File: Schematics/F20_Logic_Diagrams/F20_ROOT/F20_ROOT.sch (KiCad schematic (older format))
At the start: 0 parts

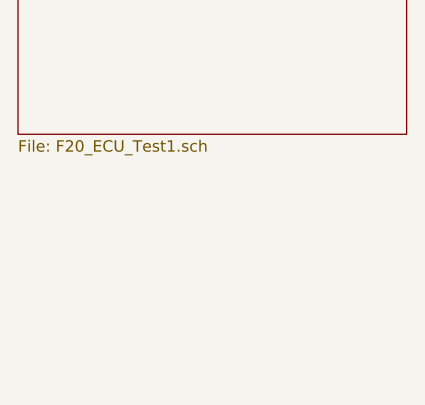
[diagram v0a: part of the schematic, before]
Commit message: Added Driver Display schematic. Added relevant symbols.
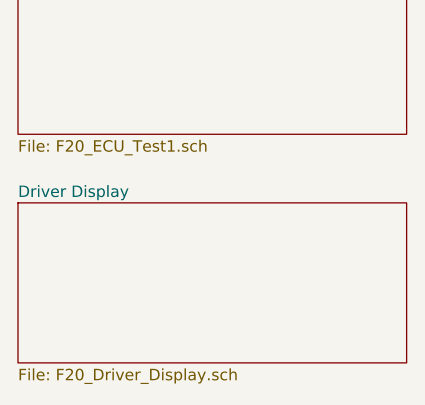
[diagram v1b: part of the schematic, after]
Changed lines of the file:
@@
 EESchema Schematic File Version 4
-LIBS:F20_ROOT-cache
 EELAYER 30 0
 EELAYER END
 $Descr A4 11693 8268
 encoding utf-8
-Sheet 1 4
+Sheet 1 5
 Title "Root Index"
 Date ""
@@
 F1 "F20_ECU_Test1.sch" 50
 $EndSheet
+$Sheet
+S 1000 4000 1700 700
+U 5E28FC41
+F0 "Driver Display" 50
+F1 "F20_Driver_Display.sch" 50
+$EndSheet
 $EndSCHEMATC

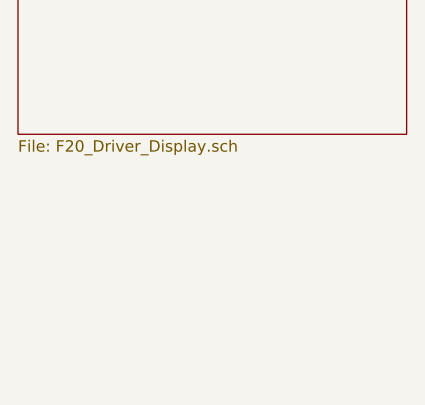
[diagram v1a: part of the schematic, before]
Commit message: Added Brakes logic diagram draft, finished charging/starting schematic portion, added relevant library parts, updated README.
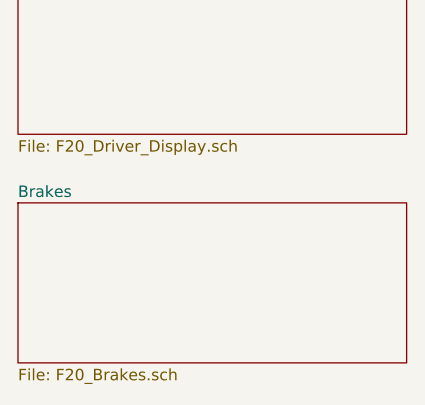
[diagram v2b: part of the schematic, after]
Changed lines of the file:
@@
 EESchema Schematic File Version 4
+LIBS:F20_ROOT-cache
 EELAYER 30 0
 EELAYER END
 $Descr A4 11693 8268
 encoding utf-8
-Sheet 1 5
+Sheet 1 6
 Title "Root Index"
 Date ""
@@
 F1 "F20_Driver_Display.sch" 50
 $EndSheet
+$Sheet
+S 1000 5000 1700 700
+U 5E30D161
+F0 "Brakes" 50
+F1 "F20_Brakes.sch" 50
+$EndSheet
 $EndSCHEMATC

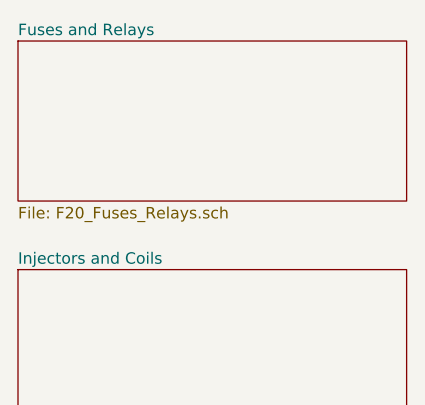
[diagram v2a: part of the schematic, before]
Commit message: Updated Brakes diagram. Updated power management diagram. Updated relevant library symbols. Updated README.
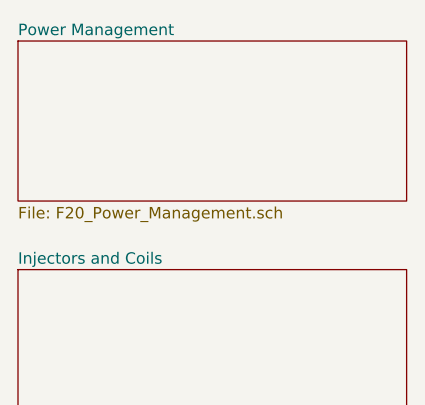
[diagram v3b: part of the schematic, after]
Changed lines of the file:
@@
 $Descr A4 11693 8268
 encoding utf-8
-Sheet 1 6
+Sheet 1 7
 Title "Root Index"
 Date ""
@@
 Comment4 ""
 $EndDescr
-$Sheet
-S 1000 1000 1700 700
-U 5E1D1A8A
-F0 "Fuses and Relays" 50
-F1 "F20_Fuses_Relays.sch" 50
-$EndSheet
 $Sheet
 S 1000 2000 1700 700
@@
 F1 "F20_Brakes.sch" 50
 $EndSheet
+$Sheet
+S 1000 1000 1700 700
+U 5E1D1A8A
+F0 "Power Management" 50
+F1 "F20_Power_Management.sch" 50
+$EndSheet
 $EndSCHEMATC

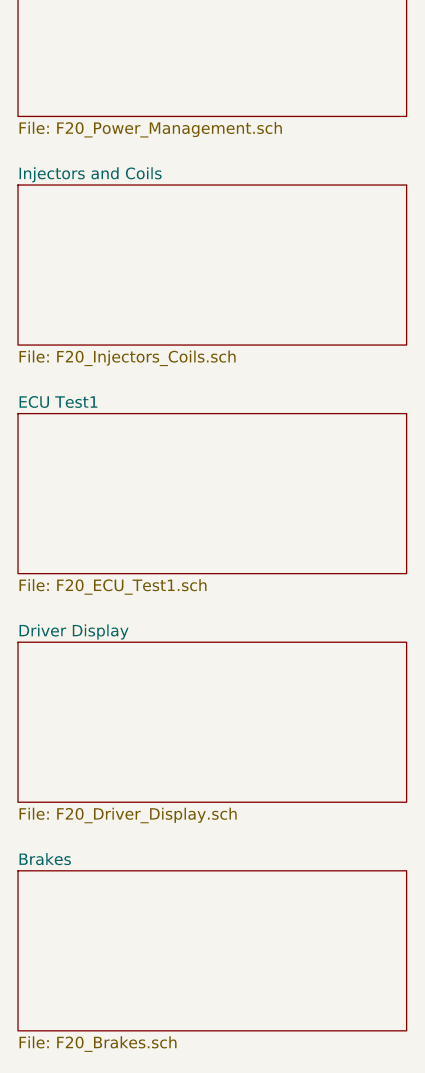
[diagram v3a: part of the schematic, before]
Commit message: Added GND and GND_CHASSIS symbols, updated relevant schematics. Restructured Powertrain hierarchy. Created ECU Connector symbols.
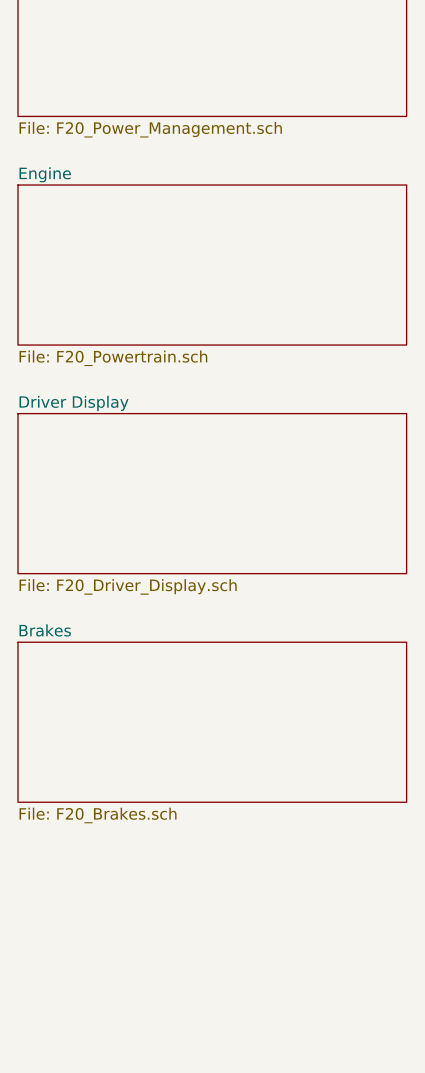
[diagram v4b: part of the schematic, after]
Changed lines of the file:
@@
 S 1000 2000 1700 700
 U 5E1D1B45
-F0 "Injectors and Coils" 50
-F1 "F20_Injectors_Coils.sch" 50
+F0 "Engine" 50
+F1 "F20_Powertrain.sch" 50
 $EndSheet
 $Sheet
 S 1000 3000 1700 700
-U 5E1D1BB2
-F0 "ECU Test1" 50
-F1 "F20_ECU_Test1.sch" 50
-$EndSheet
-$Sheet
-S 1000 4000 1700 700
 U 5E28FC41
 F0 "Driver Display" 50
@@
 $EndSheet
 $Sheet
-S 1000 5000 1700 700
+S 1000 4000 1700 700
 U 5E30D161
 F0 "Brakes" 50

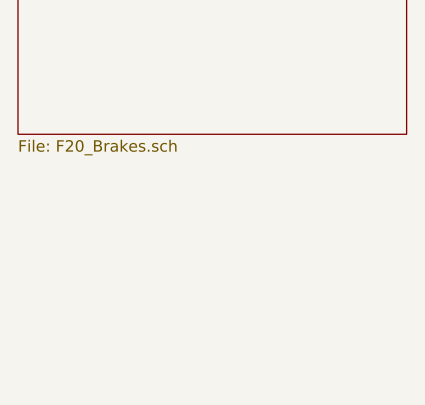
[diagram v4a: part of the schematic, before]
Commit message: Updated per AD commit. O2 sensor schematic, transponder schematic.
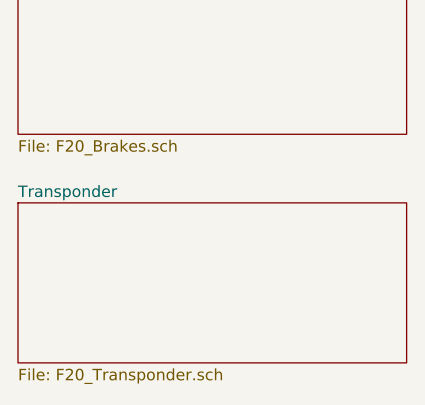
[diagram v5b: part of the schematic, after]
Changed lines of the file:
@@
 EESchema Schematic File Version 4
-LIBS:F20_ROOT-cache
 EELAYER 30 0
 EELAYER END
 $Descr A4 11693 8268
 encoding utf-8
-Sheet 1 7
+Sheet 1 9
 Title "Root Index"
 Date ""
@@
 F1 "F20_Power_Management.sch" 50
 $EndSheet
+$Sheet
+S 1000 5000 1700 700
+U 5E38F452
+F0 "Transponder" 50
+F1 "F20_Transponder.sch" 50
+$EndSheet
 $EndSCHEMATC

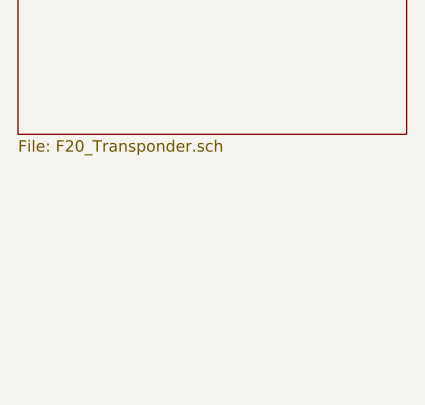
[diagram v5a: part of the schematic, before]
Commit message: Weekly update. Added Tire temp sensors drawing.
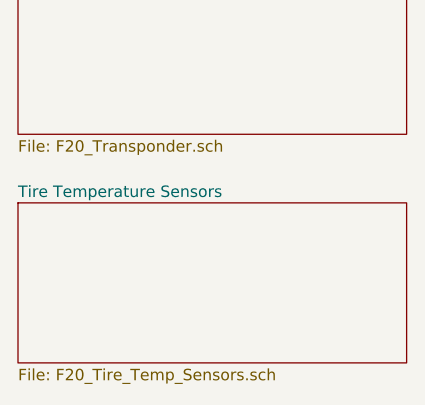
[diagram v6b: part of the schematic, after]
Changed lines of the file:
@@
 EESchema Schematic File Version 4
+LIBS:F20_ROOT-cache
 EELAYER 30 0
 EELAYER END
 $Descr A4 11693 8268
 encoding utf-8
-Sheet 1 9
+Sheet 1 11
 Title "Root Index"
 Date ""
@@
 F1 "F20_Transponder.sch" 50
 $EndSheet
+$Sheet
+S 1000 6000 1700 700
+U 5E44663D
+F0 "Tire Temperature Sensors" 50
+F1 "F20_Tire_Temp_Sensors.sch" 50
+$EndSheet
 $EndSCHEMATC

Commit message: 02/18/20 update
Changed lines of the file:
@@
 $Descr A4 11693 8268
 encoding utf-8
-Sheet 1 11
+Sheet 1 13
 Title "Root Index"
 Date ""
@@
 F1 "F20_Tire_Temp_Sensors.sch" 50
 $EndSheet
+$Sheet
+S 3000 1000 1700 700
+U 5E4F7825
+F0 "RIM" 50
+F1 "F20_RIM.sch" 50
+$EndSheet
 $EndSCHEMATC

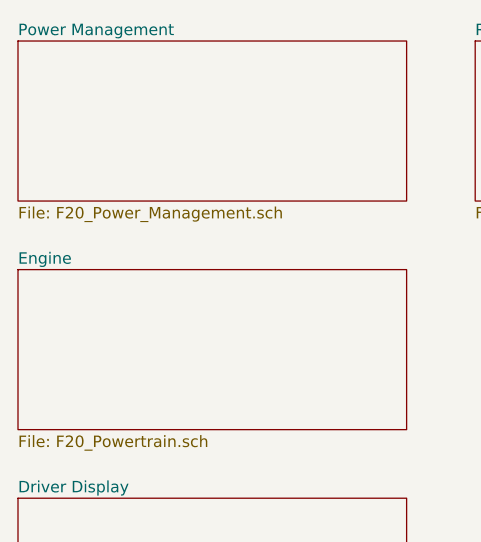
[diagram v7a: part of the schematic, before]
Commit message: Added injectors drawing
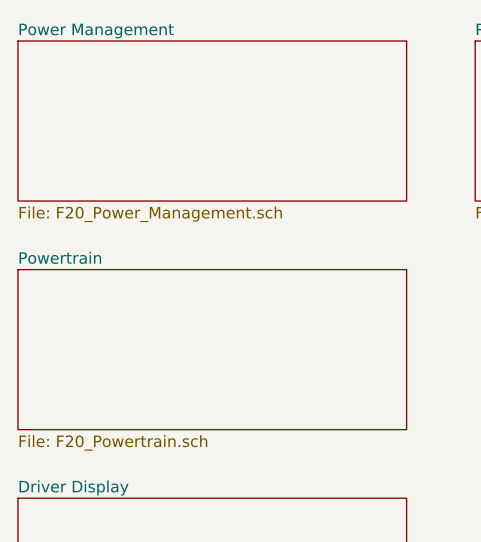
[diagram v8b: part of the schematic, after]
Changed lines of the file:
@@
 $Descr A4 11693 8268
 encoding utf-8
-Sheet 1 13
+Sheet 1 14
 Title "Root Index"
 Date ""
@@
 S 1000 2000 1700 700
 U 5E1D1B45
-F0 "Engine" 50
+F0 "Powertrain" 50
 F1 "F20_Powertrain.sch" 50
 $EndSheet
